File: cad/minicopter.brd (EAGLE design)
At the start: 25 x 25 mm, 37 parts, among them CN2 DO NOT PLACE, U1 STM32F411/48, U2 LSM6DS3, U3 DRV8835, U4 LPS25HB

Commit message: motor driver
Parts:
- removed U$2, U$3: FIDUCIAL, jaw:FIDUCIAL
- added U5: DRV8839, jaw:WSON12
- U3: value DRV8835 -> DRV8839
- moved C3 4.47 mm to (24.0, 12.0), turned to 90 degrees
- moved U3 4.03 mm to (22.5, 7.50)
- moved C23 0.56 mm to (14.0, 8.50)
- moved C4 0.50 mm to (13.0, 6.50)
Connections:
- net GND: now also U3.5, U5.5, U5.6, U5.GND3, U5.GND4, U5.GND5, U5.GND6, U5.GND7; no longer U3.11
- net IOA0: now also U5.10; no longer U3.10
- net IOA1: now also U5.8; no longer U3.9
- net IOA2: now also U3.10; no longer U3.8
- net IOA3: now also U3.8; no longer U3.7
- net N$16: now also U5.3; no longer U3.2
- net N$17: now also U5.4; no longer U3.3
- net N$19: now also U3.3; no longer U3.4
- net N$20: now also U3.4; no longer U3.5
- net VCC: now also U3.11, U3.7, U3.9, U5.11, U5.12, U5.7, U5.9
- net VCCM: now also U3.2, U5.1, U5.2
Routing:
- net VCC: track 45.5 -> 58.0 mm, vias 14 -> 17
- net GND: track 70.5 -> 80.3 mm, vias 45 -> 42
- net VCCM: track 49.7 -> 58.8 mm
- net IOA2: track 1.90 -> 4.99 mm
- net N$19: track 3.13 -> 5.16 mm
- net IOA3: track 4.05 -> 5.64 mm
- net IOA7: track 24.2 -> 22.8 mm
- net N$20: track 4.25 -> 3.23 mm
- net IOA4: track 28.2 -> 27.3 mm
- net IOA1: track 1.90 -> 2.61 mm
- net IOA0: track 1.90 -> 2.61 mm
- removed copper zone on layer 1, net VCCM

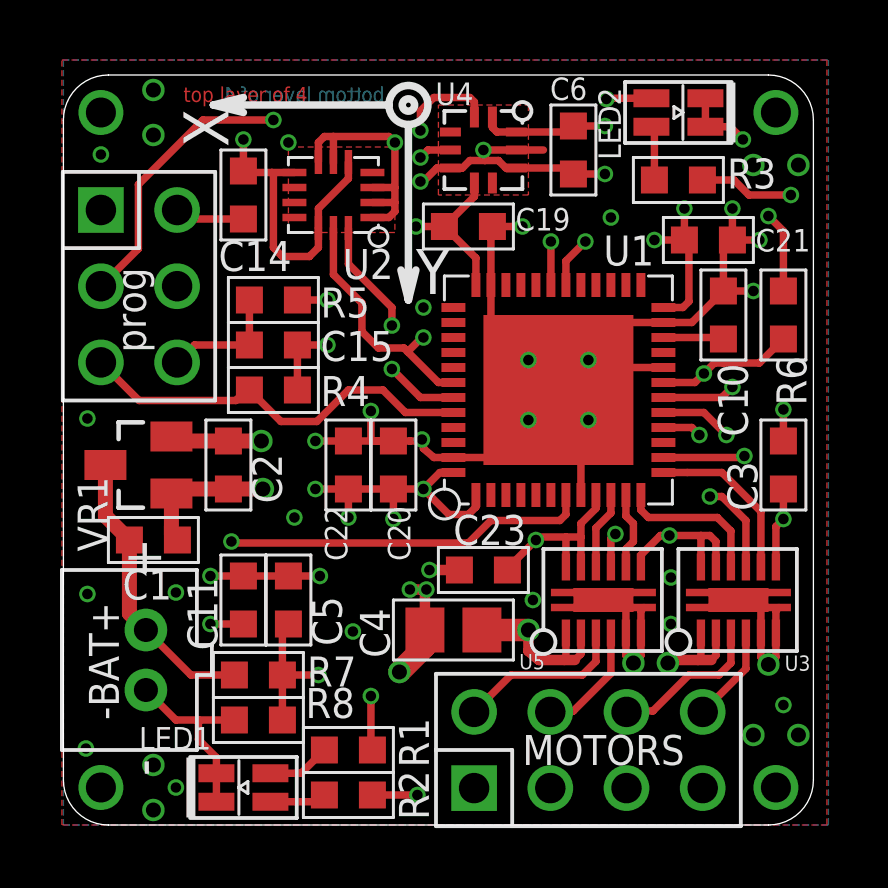
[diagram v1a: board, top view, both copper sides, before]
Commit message: add magnetometer
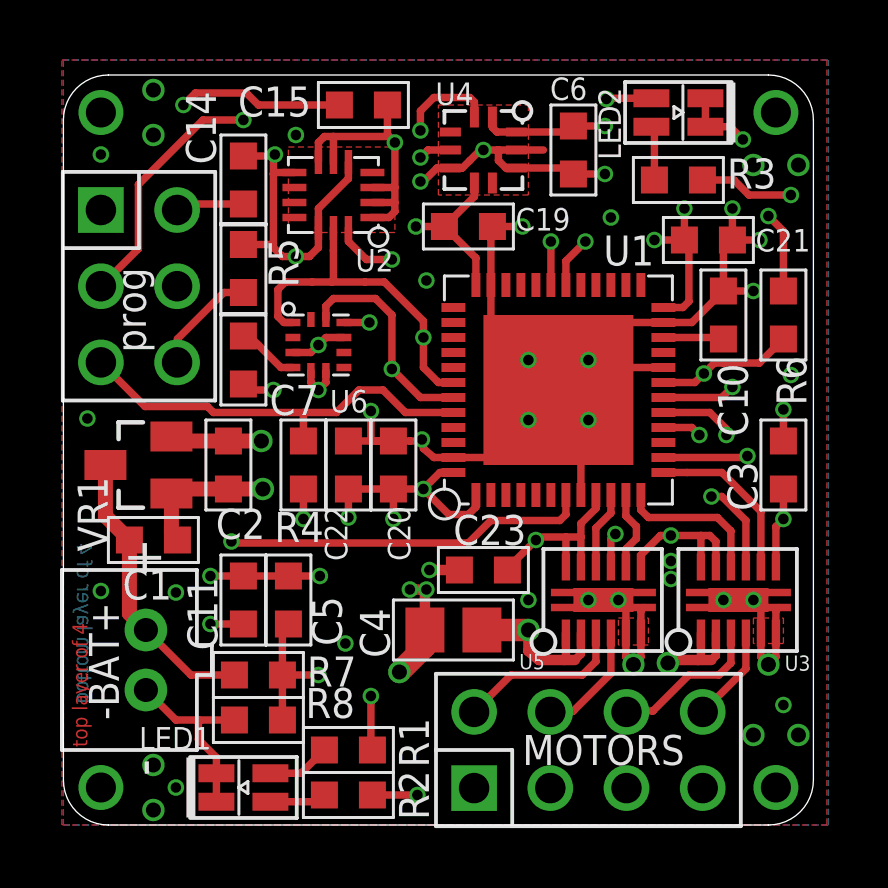
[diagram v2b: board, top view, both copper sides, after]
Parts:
- added C7: .1u, jaw:SMD0603
- added U$2: FIDUCIAL, jaw:FIDUCIAL
- added U6: LIS3MDL, jaw:LGA12
- moved C15 8.54 mm to (10.0, 24.0)
- moved R4 2.69 mm to (8.00, 12.0), turned to 90 degrees
- moved R5 1.45 mm to (6.00, 18.6), turned to 90 degrees
- moved C14 0.50 mm to (6.00, 21.5)
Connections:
- new net N$23: C7.1, U6.4
- net GND: now also C7.2, U6.3, U6.9
- net I2CCL: now also U6.1
- net I2CDA: now also U6.11
- net VCC: now also U6.10, U6.5, U6.6
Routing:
- net NRST: track 23.1 -> 37.9 mm, vias 1 -> 2
- net I2CCL: track 19.6 -> 22.8 mm
- net I2CDA: track 15.1 -> 18.1 mm
- net N$23: track 0.00 -> 2.08 mm
- net GND: track 80.3 -> 81.8 mm, vias 42 -> 46
- net VCC: track 58.0 -> 59.0 mm, vias 17 -> 18
- added copper zone on layer 1, net N$24
- added copper zone on layer 1, net N$25

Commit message: tweak
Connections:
- net GND: now also CN1.2, CN1.6; no longer CN1.1, CN1.5
- net N$16: now also CN1.1; no longer CN1.2
- net N$19: now also CN1.5; no longer CN1.6
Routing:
- net N$16: track 5.71 -> 7.98 mm
- net N$19: track 5.16 -> 7.20 mm
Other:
- board text added: "1"
- board text added: "2"
- board text added: "3"
- board text added: "4"
- board text added: "minicopter Rev. 1"
- board text removed: "minicopter Rev. 0"

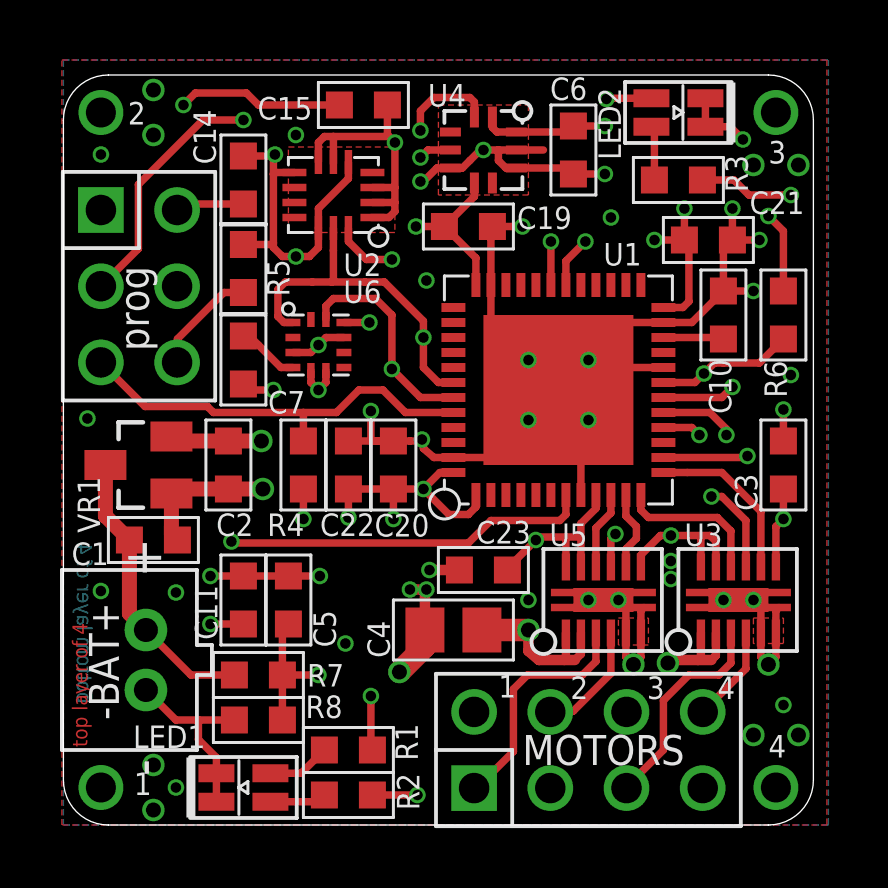
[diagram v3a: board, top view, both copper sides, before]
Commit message: add piezo
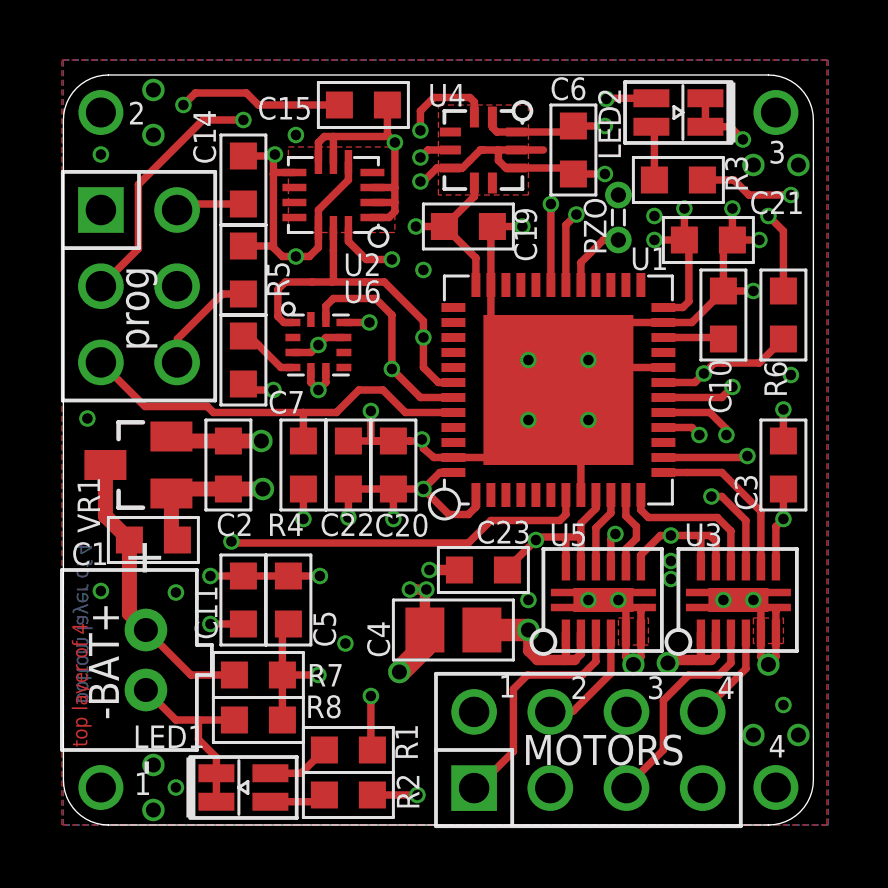
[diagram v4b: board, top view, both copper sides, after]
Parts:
- added CN4, CN5: HEADER-1X1SMALL, jaw:HEADER-1X1-SMALL
- CN2: value DO NOT PLACE -> (none)
- moved R5 0.05 mm to (6.00, 18.5)
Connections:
- new net PZ0: CN4.P$1, U1.P29
- net GND: now also CN5.P$1
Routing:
- net PZ0: track 0.00 -> 2.31 mm
- net TX: track 24.9 -> 24.4 mm
- net GND: track 81.8 -> 81.9 mm, vias 46 -> 45
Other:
- board text added: "PZO"
